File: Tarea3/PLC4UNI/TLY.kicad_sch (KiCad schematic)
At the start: 0 parts

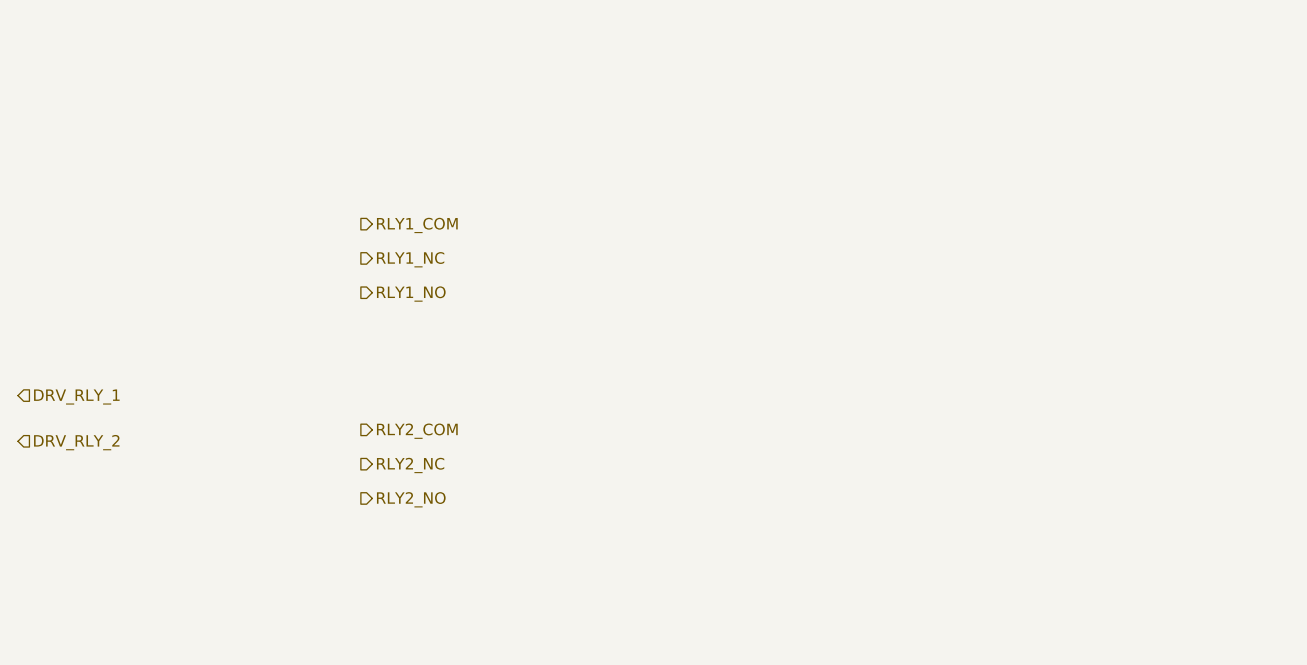
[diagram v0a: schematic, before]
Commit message: Cambio de directorio [Tarea2->CAD]
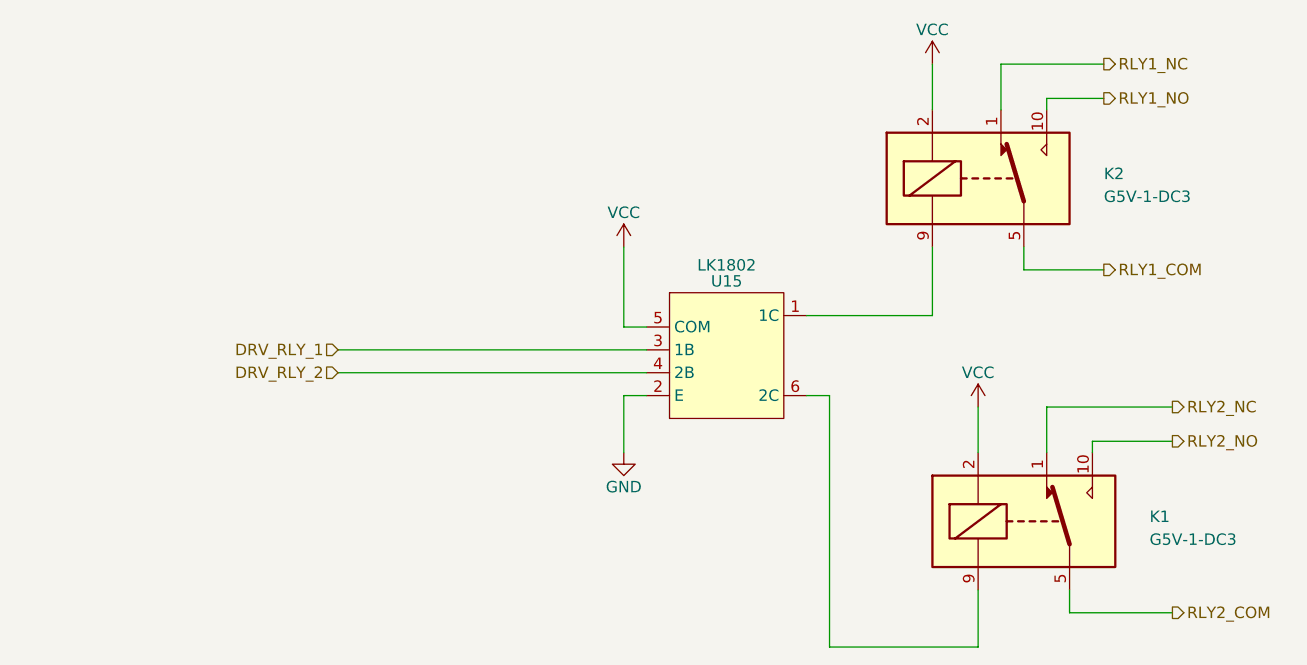
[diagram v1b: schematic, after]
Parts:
- added K1, K2: G5V-1-DC3, EasyEDA:RELAY-TH_G5V-1, symbol EasyEDA:G5V-1-DC3
- added U15: LK1802, EasyEDA:SOT-23-6_L2.9-W1.6-P0.95-LS2.8-BR, symbol EasyEDA:LK1802
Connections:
- net DRV_RLY_1: now also U15.3 (1B)
- net DRV_RLY_2: now also U15.4 (2B)
- net RLY1_COM: now also K2.5
- net RLY1_NC: now also K2.1
- net RLY1_NO: now also K2.10
- net RLY2_COM: now also K1.5
- net RLY2_NC: now also K1.1
- net RLY2_NO: now also K1.10
- new net: K2.9, U15.1 (1C)
- new net: K1.9, U15.6 (2C)
- new net GND: U15.2 (E)
- new net VCC: K1.2, K2.2, U15.5 (COM)
